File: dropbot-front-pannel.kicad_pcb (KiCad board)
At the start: 2 copper layers, 84 x 66 mm, 15 parts, among them P1 CONN_02X10, P2 CONN_02X25, P3 CONN_02X20, P4 CONN_02X25, P5 CONN_02X20, P6 CONN_02X25, P7 CONN_02X20, P8 CONN_02X10, P9 CONN_01X03

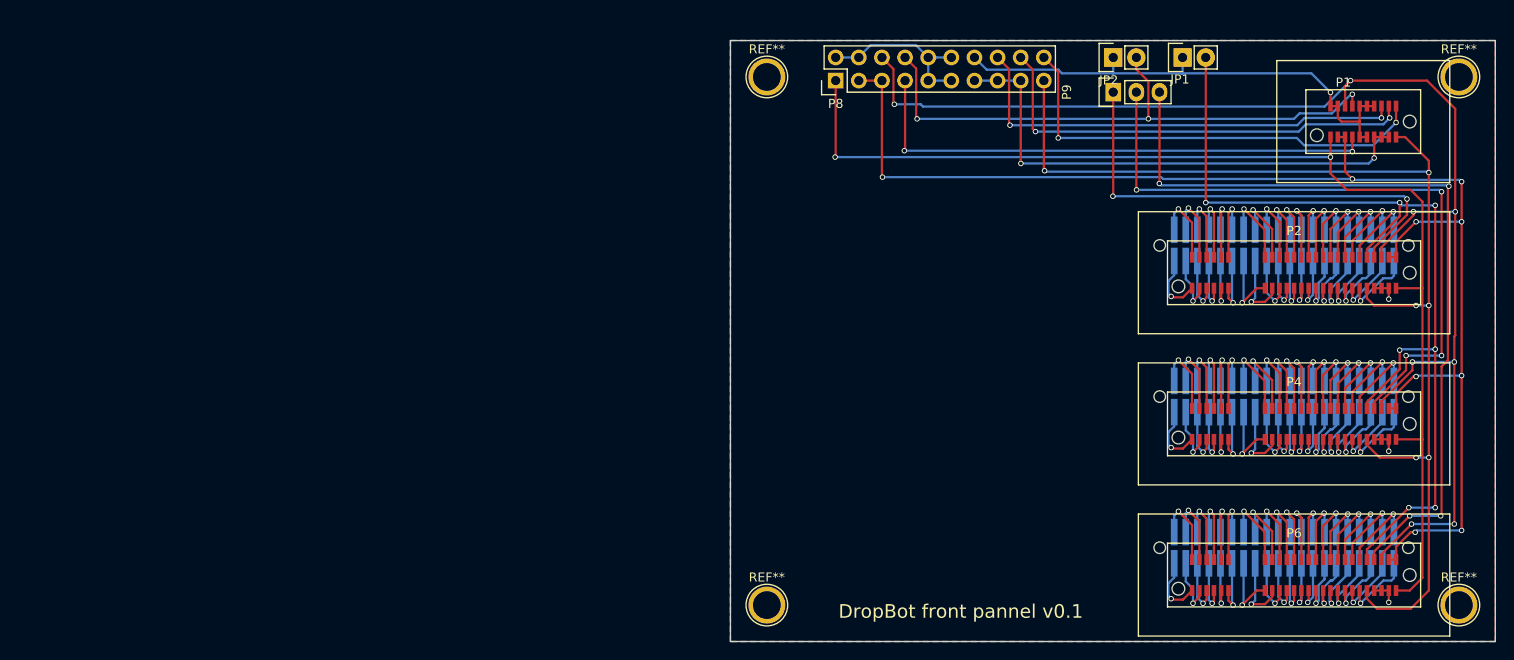
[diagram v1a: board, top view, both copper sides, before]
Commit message: [WIP] Update PCB to use Samtec connectors
Update PCB to use Samtec connectors instead of PCB edge connections.

This is because the edge connector slots are not rated for high-voltage
(i.e., they are not rated for over 30V).
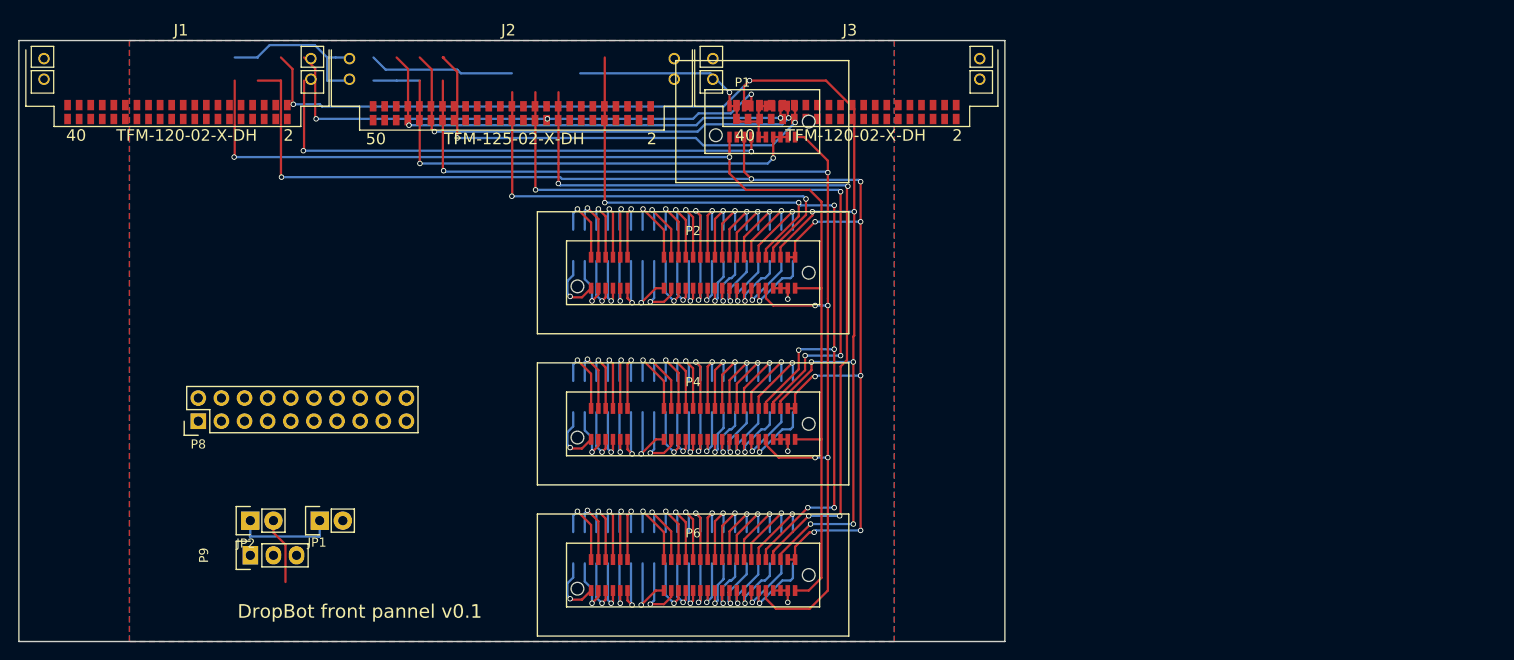
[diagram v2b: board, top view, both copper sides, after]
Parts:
- removed P3, P5, P7: CONN_02X20, WheelerLab:TFML-120-02-S-D
- removed REF** (x4): 1pin, Connect:1pin
- added J1: TFM-120-02-X-DH, WheelerLab:TFM-120-02-X-DH, F.Cu at (-36.7, 21.5)
- added J2: TFM-125-02-X-DH, WheelerLab:TFM-125-02-X-DH, F.Cu at (0.00, 21.5)
- added J3: TFM-120-02-X-DH, WheelerLab:TFM-120-02-X-DH, F.Cu at (36.7, 21.5)
- moved JP1 107.6 mm to (-21.1, 73.7)
- moved JP2 107.6 mm to (-28.7, 73.7)
- moved P9 107.6 mm to (-28.7, 77.5)
- moved P8 79.4 mm to (-34.4, 62.8)
- moved P1 66.0 mm to (27.5, 29.9)
- moved P2 66.0 mm to (19.9, 46.5)
- moved P4 66.0 mm to (19.9, 63.1)
- moved P6 66.0 mm to (19.9, 79.7)
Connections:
- P1 pad 19: HV -> HVAC
- P2 pad 41: HV -> HVAC
- P4 pad 41: HV -> HVAC
- P6 pad 41: HV -> HVAC
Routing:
- net HVAC: track 0.00 -> 129.3 mm, vias 0 -> 6
- net HV: track 129.3 -> 0.00 mm, vias 6 -> 0
- net HV_OE: track 64.8 -> 7.29 mm, vias 3 -> 0
- net Net-(J2-Pad20): track 0.00 -> 56.2 mm, vias 0 -> 3
- net +5V: track 50.0 -> 0.00 mm, vias 2 -> 0
- net D-: track 50.4 -> 1.30 mm, vias 2 -> 0
- net Net-(J3-Pad30): track 0.00 -> 48.2 mm, vias 0 -> 2
- net Net-(J2-Pad44): track 0.00 -> 40.7 mm, vias 0 -> 1
- net (no net): track 0.00 -> 39.9 mm
- net GND: track 84.1 -> 45.3 mm
- net Net-(J3-Pad19): track 0.00 -> 33.9 mm, vias 0 -> 2
- net SCL: track 150.7 -> 116.8 mm, vias 8 -> 6
- net Net-(J3-Pad32): track 0.00 -> 8.45 mm, vias 0 -> 1
- net +12V: track 57.1 -> 52.1 mm
- net Net-(J3-Pad36): track 0.00 -> 2.00 mm
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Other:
- board size 84 x 66 mm -> 108.3 x 66 mm

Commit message: Add PCB cut-aways for box stand-offs
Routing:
- net Net-(J3-Pad19): track 33.9 -> 15.7 mm, vias 2 -> 0
- net SCL: track 116.8 -> 135.0 mm, vias 6 -> 8
- net Net-(J3-Pad32): track 8.45 -> 0.00 mm
- net Net-(J2-Pad44): track 40.7 -> 49.1 mm
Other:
- outline, holes or cut-outs redrawn
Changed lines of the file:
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@@
   (general
     (links 61)
-    (no_connects 19)
-    (area -54.215101 20.924999 54.215101 87.075001)
+    (no_connects 18)
+    (area -56.626101 18.723 56.626101 87.075001)
     (thickness 1.6)
-    (drawings 5)
+    (drawings 9)
     (tracks 954)
     (zones 0)
@@
       (net 273 "Net-(J3-PadG4)"))
   )
+  (gr_line (start 54.1401 79) (end 49.1401 79) (angle 90) (layer Edge.Cuts) (width 0.15))
+  (gr_line (start 49.1401 79) (end 49.1401 87) (angle 90) (layer Edge.Cuts) (width 0.15))
+  (gr_line (start -49.1401 79) (end -49.1401 87) (angle 90) (layer Edge.Cuts) (width 0.15))
+  (gr_line (start -54.1401 79) (end -49.1401 79) (angle 90) (layer Edge.Cuts) (width 0.15))
   (gr_text "DropBot front pannel v0.1" (at -16.7 83.7) (layer F.SilkS)
     (effects (font (size 1.5 1.5) (thickness 0.3)))
   )
-  (gr_line (start 54.1401 87) (end 54.1401 21) (angle 90) (layer Edge.Cuts) (width 0.15))
-  (gr_line (start -54.1401 87) (end -54.1401 21) (angle 90) (layer Edge.Cuts) (width 0.15))
-  (gr_line (start 54.1401 87) (end -54.1401 87) (angle 90) (layer Edge.Cuts) (width 0.15))
+  (gr_line (start 54.1401 79) (end 54.1401 21) (angle 90) (layer Edge.Cuts) (width 0.15))
+  (gr_line (start -54.1401 79) (end -54.1401 21) (angle 90) (layer Edge.Cuts) (width 0.15))
+  (gr_line (start 49.1401 87) (end -49.1401 87) (angle 90) (layer Edge.Cuts) (width 0.15))
   (gr_line (start -54.1401 21) (end 54.1401 21) (angle 90) (layer Edge.Cuts) (width 0.15))
   (segment (start -13.86 24.2) (end -15.2 22.86) (width 0.25) (layer B.Cu) (net 0))
@@
   (segment (start 33 40.2) (end 33 39.8) (width 0.25) (layer F.Cu) (net 3))
   (segment (start 37.5 53.5) (end 37.6 53.4) (width 0.25) (layer F.Cu) (net 3))
+  (via (at 37.6 39.8) (size 0.6) (drill 0.4) (layers F.Cu B.Cu) (net 3))
+  (segment (start 33 39.8) (end 37.6 39.8) (width 0.25) (layer B.Cu) (net 3))
+  (via (at 33 39.8) (size 0.6) (drill 0.4) (layers F.Cu B.Cu) (net 3))
+  (segment (start 37.6 53.4) (end 37.6 39.8) (width 0.25) (layer F.Cu) (net 3))
   (segment (start 30.3 81.4) (end 30.3 82.7) (width 0.25) (layer F.Cu) (net 4))
   (via (at 30.3 82.7) (size 0.6) (drill 0.4) (layers F.Cu B.Cu) (net 4))
@@
   (segment (start 20.249998 30.3) (end -11.3 30.3) (width 0.25) (layer B.Cu) (net 223))
   (segment (start 21.049998 29.5) (end 20.249998 30.3) (width 0.25) (layer B.Cu) (net 223))
-  (via (at 37.6 39.8) (size 0.6) (drill 0.4) (layers F.Cu B.Cu) (net 248))
-  (segment (start 33 39.8) (end 37.6 39.8) (width 0.25) (layer B.Cu) (net 248))
-  (via (at 33 39.8) (size 0.6) (drill 0.4) (layers F.Cu B.Cu) (net 248))
+  (segment (start 29.5 29.5) (end 21.049998 29.5) (width 0.25) (layer B.Cu) (net 223))
   (segment (start 37.6 28.5) (end 34.5 25.4) (width 0.25) (layer F.Cu) (net 248))
-  (segment (start 37.6 53.4) (end 37.6 39.8) (width 0.25) (layer F.Cu) (net 248))
   (segment (start 37.6 39.8) (end 37.6 28.5) (width 0.25) (layer F.Cu) (net 248))
   (segment (start 31.1 28.2) (end 31.1 30) (width 0.25) (layer F.Cu) (net 258))
@@
   (segment (start -6 31.7) (end -5.95 31.65) (width 0.25) (layer F.Cu) (net 259))
   (segment (start -7.44 22.86) (end -7.58 22.86) (width 0.25) (layer F.Cu) (net 259))
-  (segment (start 29.5 29.5) (end 21.049998 29.5) (width 0.25) (layer B.Cu) (net 261))
   (via (at 29.5 29.5) (size 0.6) (drill 0.4) (layers F.Cu B.Cu) (net 261))
   (segment (start 25.1 29.9) (end 27.1 29.9) (width 0.25) (layer F.Cu) (net 265))

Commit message: Increase height of PCB to match dims of box
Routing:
- net Net-(J3-Pad19): track 15.7 -> 20.3 mm, vias 0 -> 1
- net SCL: track 135.0 -> 130.4 mm, vias 8 -> 7
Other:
- board size 108.3 x 66 mm -> 108.3 x 68.8 mm
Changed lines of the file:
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@@
   (general
     (links 61)
-    (no_connects 18)
+    (no_connects 19)
     (area -56.626101 18.723 56.626101 87.075001)
     (thickness 1.6)
@@
       (net 273 "Net-(J3-PadG4)"))
   )
-  (gr_line (start 54.1401 79) (end 49.1401 79) (angle 90) (layer Edge.Cuts) (width 0.15))
-  (gr_line (start 49.1401 79) (end 49.1401 87) (angle 90) (layer Edge.Cuts) (width 0.15))
-  (gr_line (start -49.1401 79) (end -49.1401 87) (angle 90) (layer Edge.Cuts) (width 0.15))
-  (gr_line (start -54.1401 79) (end -49.1401 79) (angle 90) (layer Edge.Cuts) (width 0.15))
+  (gr_line (start 54.1401 81.75) (end 49.1401 81.75) (angle 90) (layer Edge.Cuts) (width 0.15))
+  (gr_line (start 49.1401 81.75) (end 49.1401 89.75) (angle 90) (layer Edge.Cuts) (width 0.15))
+  (gr_line (start -49.1401 81.75) (end -49.1401 89.75) (angle 90) (layer Edge.Cuts) (width 0.15))
+  (gr_line (start -54.1401 81.75) (end -49.1401 81.75) (angle 90) (layer Edge.Cuts) (width 0.15))
   (gr_text "DropBot front pannel v0.1" (at -16.7 83.7) (layer F.SilkS)
     (effects (font (size 1.5 1.5) (thickness 0.3)))
   )
-  (gr_line (start 54.1401 79) (end 54.1401 21) (angle 90) (layer Edge.Cuts) (width 0.15))
-  (gr_line (start -54.1401 79) (end -54.1401 21) (angle 90) (layer Edge.Cuts) (width 0.15))
-  (gr_line (start 49.1401 87) (end -49.1401 87) (angle 90) (layer Edge.Cuts) (width 0.15))
+  (gr_line (start 54.1401 81.75) (end 54.1401 21) (angle 90) (layer Edge.Cuts) (width 0.15))
+  (gr_line (start -54.1401 81.75) (end -54.1401 21) (angle 90) (layer Edge.Cuts) (width 0.15))
+  (gr_line (start 49.1401 89.75) (end -49.1401 89.75) (angle 90) (layer Edge.Cuts) (width 0.15))
   (gr_line (start -54.1401 21) (end 54.1401 21) (angle 90) (layer Edge.Cuts) (width 0.15))
   (segment (start -13.86 24.2) (end -15.2 22.86) (width 0.25) (layer B.Cu) (net 0))
@@
   (segment (start 33 40.2) (end 33 39.8) (width 0.25) (layer F.Cu) (net 3))
   (segment (start 37.5 53.5) (end 37.6 53.4) (width 0.25) (layer F.Cu) (net 3))
-  (via (at 37.6 39.8) (size 0.6) (drill 0.4) (layers F.Cu B.Cu) (net 3))
-  (segment (start 33 39.8) (end 37.6 39.8) (width 0.25) (layer B.Cu) (net 3))
   (via (at 33 39.8) (size 0.6) (drill 0.4) (layers F.Cu B.Cu) (net 3))
   (segment (start 37.6 53.4) (end 37.6 39.8) (width 0.25) (layer F.Cu) (net 3))
@@
   (segment (start 21.049998 29.5) (end 20.249998 30.3) (width 0.25) (layer B.Cu) (net 223))
   (segment (start 29.5 29.5) (end 21.049998 29.5) (width 0.25) (layer B.Cu) (net 223))
+  (via (at 37.6 39.8) (size 0.6) (drill 0.4) (layers F.Cu B.Cu) (net 248))
+  (segment (start 33 39.8) (end 37.6 39.8) (width 0.25) (layer B.Cu) (net 248))
   (segment (start 37.6 28.5) (end 34.5 25.4) (width 0.25) (layer F.Cu) (net 248))
   (segment (start 37.6 39.8) (end 37.6 28.5) (width 0.25) (layer F.Cu) (net 248))
